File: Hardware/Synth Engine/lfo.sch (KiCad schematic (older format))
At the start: 29 parts, among them U4 TL074, U5 TL074

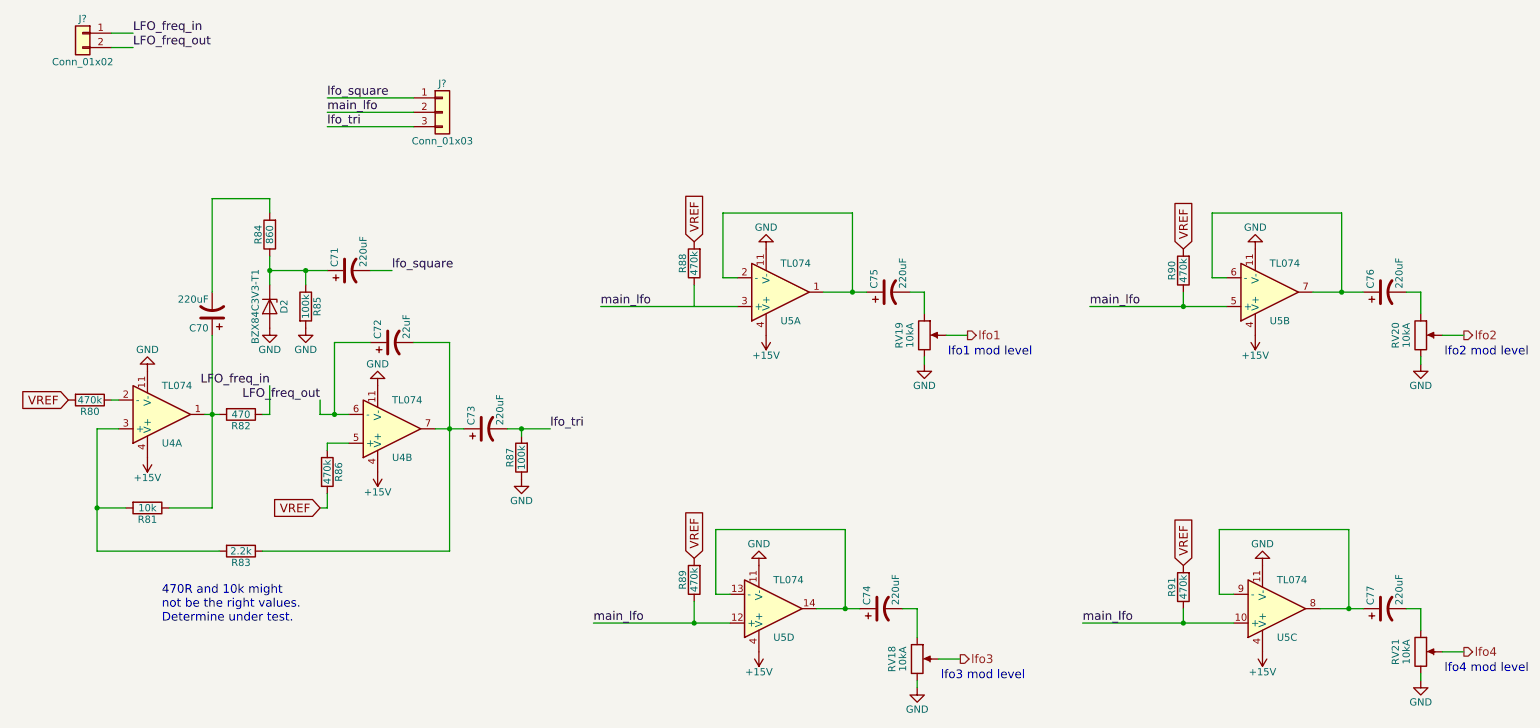
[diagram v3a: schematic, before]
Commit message: remove external pull-up resistors on digital input pins. These are unecessary due to internal pull-up resistors.
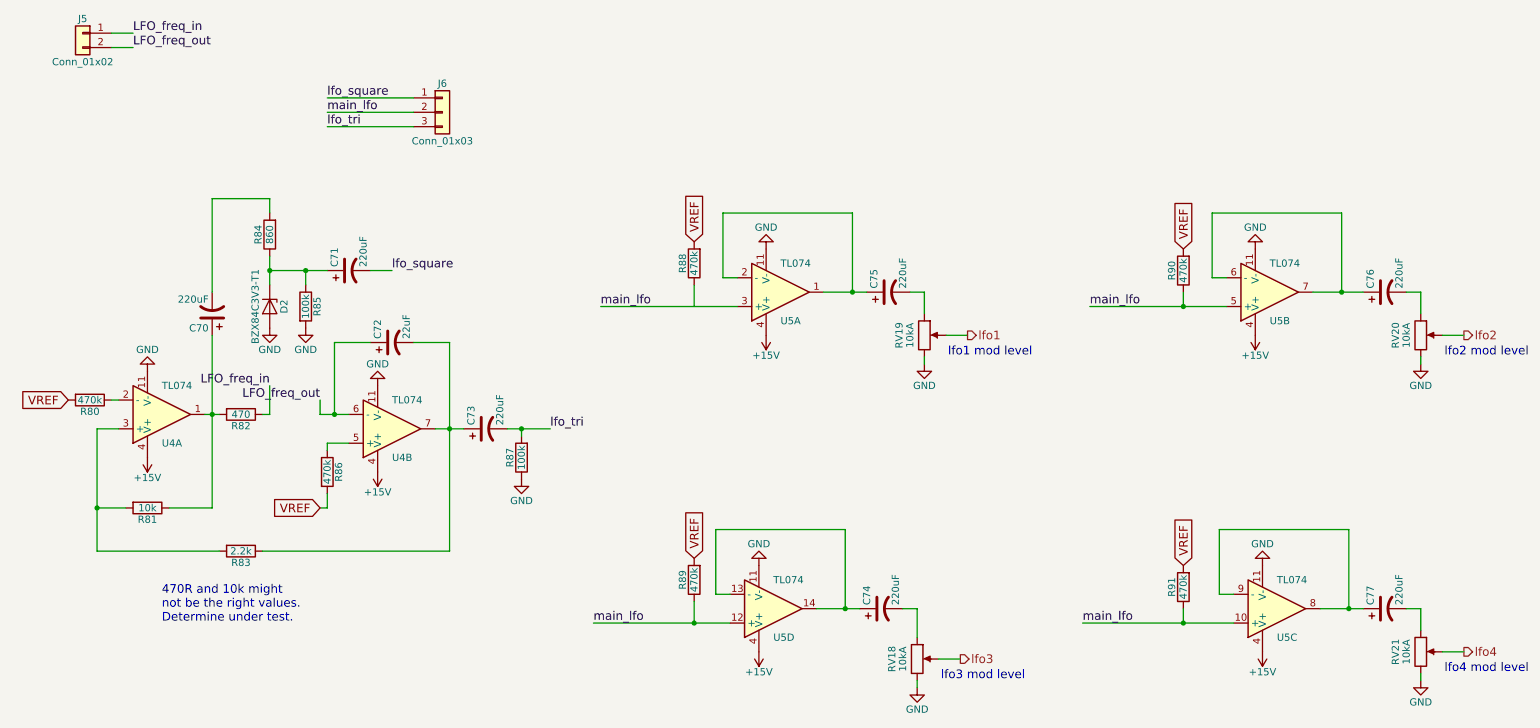
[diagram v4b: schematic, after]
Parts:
- J5: renamed from J?; footprint (none) -> Pin_Headers:Pin_Header_Straight_1x02_Pitch2.54mm
- J6: renamed from J?; footprint (none) -> Pin_Headers:Pin_Header_Straight_1x03_Pitch2.54mm
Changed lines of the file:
@@
 lfo4
 $Comp
-L GND #PWR092
+L GND #PWR088
 U 1 1 5C37F537
 P 1450 3300
-F 0 "#PWR092" H 1450 3050 50  0001 C CNN
+F 0 "#PWR088" H 1450 3050 50  0001 C CNN
 F 1 "GND" H 1450 3150 50  0000 C CNN
 F 2 "" H 1450 3300 50  0001 C CNN
@@
 $EndComp
 $Comp
-L GND #PWR093
+L GND #PWR089
 U 1 1 5C37F5BA
 P 3050 3400
-F 0 "#PWR093" H 3050 3150 50  0001 C CNN
+F 0 "#PWR089" H 3050 3150 50  0001 C CNN
 F 1 "GND" H 3050 3250 50  0000 C CNN
 F 2 "" H 3050 3400 50  0001 C CNN
@@
 $EndComp
 $Comp
-L +15V #PWR094
+L +15V #PWR090
 U 1 1 5C37FA4D
 P 1450 3900
-F 0 "#PWR094" H 1450 3750 50  0001 C CNN
+F 0 "#PWR090" H 1450 3750 50  0001 C CNN
 F 1 "+15V" H 1450 4040 50  0000 C CNN
 F 2 "" H 1450 3900 50  0001 C CNN
@@
 $EndComp
 $Comp
-L +15V #PWR095
+L +15V #PWR091
 U 1 1 5C37FAD0
 P 3050 4000
-F 0 "#PWR095" H 3050 3850 50  0001 C CNN
+F 0 "#PWR091" H 3050 3850 50  0001 C CNN
 F 1 "+15V" H 3050 4140 50  0000 C CNN
 F 2 "" H 3050 4000 50  0001 C CNN
@@
 $EndComp
 $Comp
-L GND #PWR096
+L GND #PWR092
 U 1 1 5C381B69
 P 4050 4050
-F 0 "#PWR096" H 4050 3800 50  0001 C CNN
+F 0 "#PWR092" H 4050 3800 50  0001 C CNN
 F 1 "GND" H 4050 3900 50  0000 C CNN
 F 2 "" H 4050 4050 50  0001 C CNN
@@
 $EndComp
 $Comp
-L GND #PWR097
+L GND #PWR093
 U 1 1 5C38F259
 P 2300 3000
-F 0 "#PWR097" H 2300 2750 50  0001 C CNN
+F 0 "#PWR093" H 2300 2750 50  0001 C CNN
 F 1 "GND" H 2300 2850 50  0000 C CNN
 F 2 "" H 2300 3000 50  0001 C CNN
@@
 $EndComp
 $Comp
-L GND #PWR098
+L GND #PWR094
 U 1 1 5C50BC49
 P 2550 3000
-F 0 "#PWR098" H 2550 2750 50  0001 C CNN
+F 0 "#PWR094" H 2550 2750 50  0001 C CNN
 F 1 "GND" H 2550 2850 50  0000 C CNN
 F 2 "" H 2550 3000 50  0001 C CNN
@@
 lfo4 mod level
 $Comp
-L GND #PWR099
+L GND #PWR095
 U 1 1 5C375075
 P 10300 5450
-F 0 "#PWR099" H 10300 5200 50  0001 C CNN
+F 0 "#PWR095" H 10300 5200 50  0001 C CNN
 F 1 "GND" H 10300 5300 50  0000 C CNN
 F 2 "" H 10300 5450 50  0001 C CNN
@@
 lfo2 mod level
 $Comp
-L GND #PWR0100
+L GND #PWR096
 U 1 1 5C374D0F
 P 10300 3250
-F 0 "#PWR0100" H 10300 3000 50  0001 C CNN
+F 0 "#PWR096" H 10300 3000 50  0001 C CNN
 F 1 "GND" H 10300 3100 50  0000 C CNN
 F 2 "" H 10300 3250 50  0001 C CNN
@@
 lfo3 mod level
 $Comp
-L GND #PWR0101
+L GND #PWR097
 U 1 1 5C374E52
 P 6800 5500
-F 0 "#PWR0101" H 6800 5250 50  0001 C CNN
+F 0 "#PWR097" H 6800 5250 50  0001 C CNN
 F 1 "GND" H 6800 5350 50  0000 C CNN
 F 2 "" H 6800 5500 50  0001 C CNN
@@
 lfo1 mod level
 $Comp
-L GND #PWR0102
+L GND #PWR098
 U 1 1 5C3694AC
 P 6850 3250
-F 0 "#PWR0102" H 6850 3000 50  0001 C CNN
+F 0 "#PWR098" H 6850 3000 50  0001 C CNN
 F 1 "GND" H 6850 3100 50  0000 C CNN
 F 2 "" H 6850 3250 50  0001 C CNN
@@
 main_lfo
 $Comp
-L GND #PWR0103
+L GND #PWR099
 U 1 1 5C541D9A
 P 5750 2450
-F 0 "#PWR0103" H 5750 2200 50  0001 C CNN
+F 0 "#PWR099" H 5750 2200 50  0001 C CNN
 F 1 "GND" H 5750 2300 50  0000 C CNN
 F 2 "" H 5750 2450 50  0001 C CNN
@@
 $EndComp
 $Comp
-L +15V #PWR0104
+L +15V #PWR0100
 U 1 1 5C541DA0
 P 5750 3050
-F 0 "#PWR0104" H 5750 2900 50  0001 C CNN
+F 0 "#PWR0100" H 5750 2900 50  0001 C CNN
 F 1 "+15V" H 5750 3190 50  0000 C CNN
 F 2 "" H 5750 3050 50  0001 C CNN
@@
 main_lfo
 $Comp
-L GND #PWR0105
+L GND #PWR0101
 U 1 1 5C542158
 P 9150 2450
-F 0 "#PWR0105" H 9150 2200 50  0001 C CNN
+F 0 "#PWR0101" H 9150 2200 50  0001 C CNN
 F 1 "GND" H 9150 2300 50  0000 C CNN
 F 2 "" H 9150 2450 50  0001 C CNN
@@
 $EndComp
 $Comp
-L +15V #PWR0106
+L +15V #PWR0102
 U 1 1 5C54215E
 P 9150 3050
-F 0 "#PWR0106" H 9150 2900 50  0001 C CNN
+F 0 "#PWR0102" H 9150 2900 50  0001 C CNN
 F 1 "+15V" H 9150 3190 50  0000 C CNN
 F 2 "" H 9150 3050 50  0001 C CNN
@@
 main_lfo
 $Comp
-L GND #PWR0107
+L GND #PWR0103
 U 1 1 5C5423E6
 P 5700 4650
-F 0 "#PWR0107" H 5700 4400 50  0001 C CNN
+F 0 "#PWR0103" H 5700 4400 50  0001 C CNN
 F 1 "GND" H 5700 4500 50  0000 C CNN
 F 2 "" H 5700 4650 50  0001 C CNN
@@
 $EndComp
 $Comp
-L +15V #PWR0108
+L +15V #PWR0104
 U 1 1 5C5423EC
 P 5700 5250
-F 0 "#PWR0108" H 5700 5100 50  0001 C CNN
+F 0 "#PWR0104" H 5700 5100 50  0001 C CNN
 F 1 "+15V" H 5700 5390 50  0000 C CNN
 F 2 "" H 5700 5250 50  0001 C CNN
@@
 main_lfo
 $Comp
-L GND #PWR0109
+L GND #PWR0105
 U 1 1 5C5426E0
 P 9200 4650
-F 0 "#PWR0109" H 9200 4400 50  0001 C CNN
+F 0 "#PWR0105" H 9200 4400 50  0001 C CNN
 F 1 "GND" H 9200 4500 50  0000 C CNN
 F 2 "" H 9200 4650 50  0001 C CNN
@@
 $EndComp
 $Comp
-L +15V #PWR0110
+L +15V #PWR0106
 U 1 1 5C5426E6
 P 9200 5250
-F 0 "#PWR0110" H 9200 5100 50  0001 C CNN
+F 0 "#PWR0106" H 9200 5100 50  0001 C CNN
 F 1 "+15V" H 9200 5390 50  0000 C CNN
 F 2 "" H 9200 5250 50  0001 C CNN
@@
 	10200 4950 10300 4950
 Wire Wire Line
-	9600 4950 9800 4950
-Wire Wire Line
-	9800 4950 9900 4950
+	9600 4950 9900 4950
 Wire Wire Line
 	10200 2750 10300 2750
 Wire Wire Line
-	9550 2750 9750 2750
-Wire Wire Line
-	9750 2750 9900 2750
+	9550 2750 9900 2750
 Wire Wire Line
 	6700 4950 6800 4950
 Wire Wire Line
-	6100 4950 6300 4950
-Wire Wire Line
-	6300 4950 6400 4950
+	6100 4950 6400 4950
 Wire Wire Line
 	6750 2750 6850 2750
 Wire Wire Line
-	6150 2750 6350 2750
-Wire Wire Line
-	6350 2750 6450 2750
+	6150 2750 6450 2750
 Connection ~ 8650 5050
 Wire Wire Line
@@
 	9800 4950 9800 4400
 Wire Wire Line
-	7950 5050 8650 5050
-Wire Wire Line
-	8650 5050 9000 5050
+	7950 5050 9000 5050
 Connection ~ 6300 4950
 Wire Wire Line
@@
 	6300 4950 6300 4400
 Wire Wire Line
-	4550 5050 5250 5050
-Wire Wire Line
-	5250 5050 5500 5050
+	4550 5050 5500 5050
 Connection ~ 9750 2750
 Wire Wire Line
@@
 	9750 2750 9750 2200
 Wire Wire Line
-	8000 2850 8650 2850
-Wire Wire Line
-	8650 2850 8950 2850
+	8000 2850 8950 2850
 Connection ~ 6350 2750
 Wire Wire Line
@@
 Connection ~ 2300 2600
 Wire Wire Line
-	2300 2600 2550 2600
-Wire Wire Line
-	2550 2600 2700 2600
+	2300 2600 2700 2600
 Wire Wire Line
 	2300 2100 2300 2200
@@
 	1900 2100 2300 2100
 Wire Wire Line
-	2300 2500 2300 2600
-Wire Wire Line
-	2300 2600 2300 2700
+	2300 2500 2300 2700
 Wire Wire Line
 	2700 3800 2850 3800
 Wire Wire Line
-	2650 3600 2750 3600
-Wire Wire Line
-	2750 3600 2850 3600
-Wire Wire Line
-	3450 3700 3550 3700
-Wire Wire Line
-	3550 3700 3650 3700
+	2650 3600 2850 3600
+Wire Wire Line
+	3450 3700 3650 3700
 Wire Wire Line
 	1250 3700 1100 3700
@@
 Connection ~ 4050 3700
 Wire Wire Line
-	3950 3700 4050 3700
-Wire Wire Line
-	4050 3700 4250 3700
+	3950 3700 4250 3700
 Wire Wire Line
 	4050 3750 4050 3700
@@
 	3550 4550 2250 4550
 Wire Wire Line
-	1100 3700 1100 4250
-Wire Wire Line
-	1100 4250 1100 4550
+	1100 3700 1100 4550
 Wire Wire Line
 	1300 4250 1100 4250
@@
 	1900 4250 1600 4250
 Wire Wire Line
-	1900 3050 1900 3600
-Wire Wire Line
-	1900 3600 1900 4250
+	1900 3050 1900 4250
 Wire Wire Line
 	2700 3850 2700 3800
@@
 	3550 3100 3300 3100
 Wire Wire Line
-	3550 3100 3550 3700
-Wire Wire Line
-	3550 3700 3550 4550
-Wire Wire Line
-	1850 3600 1900 3600
-Wire Wire Line
-	1900 3600 1950 3600
+	3550 3100 3550 4550
+Wire Wire Line
+	1850 3600 1950 3600
 Wire Wire Line
 	2250 3600 2300 3600
@@
 	2650 3500 2650 3600
 $Comp
-L Conn_01x03 J?
+L Conn_01x03 J6
 U 1 1 5C5E25FE
 P 3500 1500
-F 0 "J?" H 3500 1700 50  0000 C CNN
+F 0 "J6" H 3500 1700 50  0000 C CNN
 F 1 "Conn_01x03" H 3500 1300 50  0000 C CNN
-F 2 "" H 3500 1500 50  0001 C CNN
+F 2 "Pin_Headers:Pin_Header_Straight_1x03_Pitch2.54mm" H 3500 1500 50  0001 C CNN
 F 3 "" H 3500 1500 50  0001 C CNN
 	1    3500 1500
@@
 	2700 1500 3300 1500
 $Comp
-L Conn_01x02 J?
+L Conn_01x02 J5
 U 1 1 5C5E39A1
 P 1000 950
-F 0 "J?" H 1000 1050 50  0000 C CNN
+F 0 "J5" H 1000 1050 50  0000 C CNN
 F 1 "Conn_01x02" H 1000 750 50  0000 C CNN
-F 2 "" H 1000 950 50  0001 C CNN
+F 2 "Pin_Headers:Pin_Header_Straight_1x02_Pitch2.54mm" H 1000 950 50  0001 C CNN
 F 3 "" H 1000 950 50  0001 C CNN
 	1    1000 950

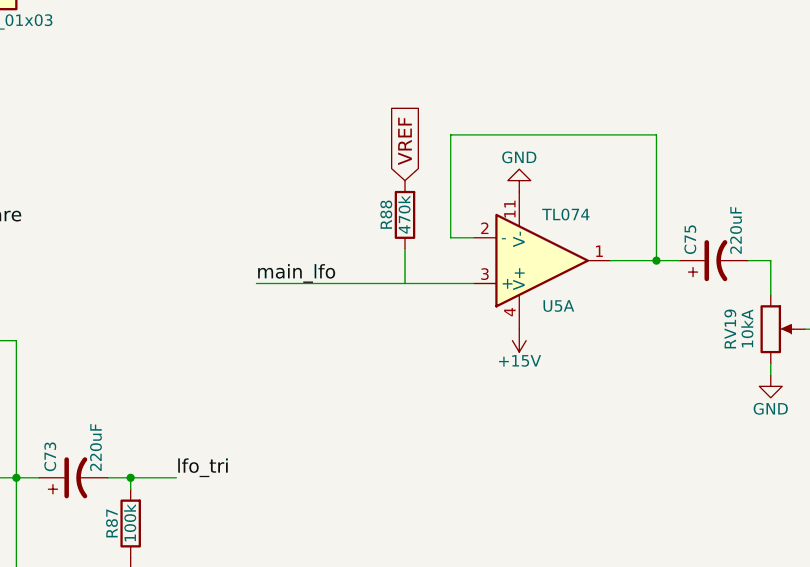
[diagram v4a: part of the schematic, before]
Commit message: place envelope footprints. all footprints loosely grouped together.
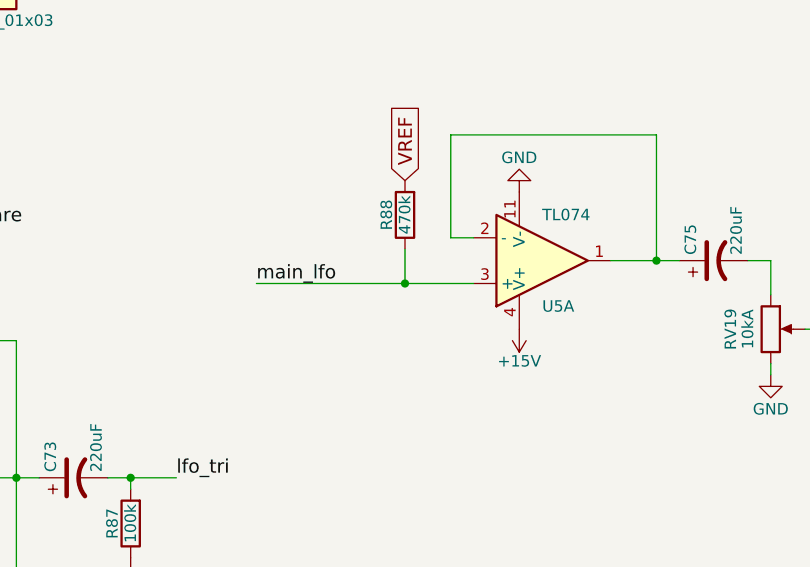
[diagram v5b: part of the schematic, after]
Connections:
- net main_lfo: now also R88.1
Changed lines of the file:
@@
 Wire Wire Line
 	3000 2600 3150 2600
-Wire Wire Line
-	5250 2700 5250 2850
 Connection ~ 9800 4950
 Wire Wire Line
@@
 Text Label 2650 3500 2    60   ~ 0
 LFO_freq_out
+Wire Wire Line
+	5250 2700 5250 2850
+Connection ~ 5250 2850
 $EndSCHEMATC
